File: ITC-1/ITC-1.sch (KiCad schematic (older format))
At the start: 84 parts, among them K1 кнопка, K2 кнопка, X1 крепеж, X2 крепеж

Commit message: упрощена схема подтяжек, раскинут разъем программирования
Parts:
- removed R19, R20, R24, R25: Резистор_0,065Вт, N_RLC:Резистор_SMD_0603_0,065_Вт_pnp, symbol elements:Резистор_0,065Вт
- added R41, R42: Резистор_0,065Вт, N_RLC:Резистор_SMD_0603_0,065_Вт_pnp, symbol elements:Резистор_0,065Вт
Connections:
- wire segments 303 -> 306
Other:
- moved on the sheet: C1, C2, G1, K1, K2, R21, R22, R32, R33, R34, R35, R36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

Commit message: раскинуты все разъемы, требуется подключить LED и поставить лого
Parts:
- removed R30, R31, R34, R35, R36: Резистор_0,065Вт, N_RLC:Резистор_SMD_0603_0,065_Вт_pnp, symbol elements:Резистор_0,065Вт
- removed VT12: Транзистор_полевой_N-IRLML6344TR, N_VD_HL:Транзистор_IRLML6344TR_SOT-23, symbol elements:Транзистор_полевой_N-IRLML6344TR
- G2: symbol MOTOR_2020_import:ИОП_LM4040BIM3-2.5_NOPB -> ITC-1-rescue:ИОП_LM4040BIM3-2.5_NOPB-MOTOR_2020_import
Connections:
- net labels removed: LED-DRIVE
- wire segments 306 -> 293
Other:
- moved on the sheet: R33, R37, R38, R39, R40

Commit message: готова трассировка, требуется контрольная проверка
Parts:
- added D1: LOGO, N_ICO:ni_10x10, symbol elements:LOGO
- added D2: LOGO, N_ICO:VLAD_10x10, symbol elements:LOGO
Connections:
- net BUTT_1: now also A1.30 (IO18); no longer A1.27 (IO16)
- net BUTT_2: now also A1.31 (IO19); no longer A1.28 (IO17)
- net LED_7: now also A1.27 (IO16); no longer A1.29 (IO5)
- net LED_8: now also A1.28 (IO17); no longer A1.30 (IO18)
- net LED_9: now also A1.29 (IO5); no longer A1.31 (IO19)
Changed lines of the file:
@@
 EESchema Schematic File Version 4
 LIBS:ITC-1-cache
-EELAYER 29 0
+EELAYER 30 0
 EELAYER END
 $Descr A2 23386 16535
@@
 Entry Wire Line
 	6500 2950 6400 3050
+Text Label 6250 3650 2    50   ~ 0
+LED_7
+Entry Wire Line
+	6500 3100 6400 3200
+Text Label 6250 3500 2    50   ~ 0
+LED_8
+Entry Wire Line
+	6500 3250 6400 3350
+Wire Wire Line
+	3100 4650 1350 4650
+Wire Wire Line
+	3100 4250 3100 4650
+Entry Wire Line
+	1250 4550 1350 4650
+Wire Wire Line
+	1500 4500 2950 4500
+Wire Wire Line
+	2950 4500 2950 4250
 Text Label 6250 3350 2    50   ~ 0
-LED_7
-Entry Wire Line
-	6500 3100 6400 3200
-Text Label 6250 3200 2    50   ~ 0
-LED_8
-Entry Wire Line
-	6500 3250 6400 3350
-Wire Wire Line
-	3100 4650 1350 4650
-Wire Wire Line
-	3100 4250 3100 4650
-Entry Wire Line
-	1250 4550 1350 4650
-Wire Wire Line
-	1500 4500 2950 4500
-Wire Wire Line
-	2950 4500 2950 4250
-Text Label 6250 3050 2    50   ~ 0
 LED_9
 Wire Wire Line
@@
 Entry Wire Line
 	6500 2900 6600 3000
-Text Label 6250 3650 2    50   ~ 0
+Text Label 6250 3200 2    50   ~ 0
 BUTT_1
-Text Label 6250 3500 2    50   ~ 0
+Text Label 6250 3050 2    50   ~ 0
 BUTT_2
 Wire Wire Line
@@
 Entry Wire Line
 	6400 3800 6500 3900
+Text Label 2875 13000 2    50   ~ 0
+3V3
+$Comp
+L elements:LOGO D1
+U 1 1 60B714C3
+P 4750 1000
+F 0 "D1" H 4675 1200 50  0001 C CNN
+F 1 "LOGO" H 4650 1000 50  0000 L CNN
+F 2 "N_ICO:ni_10x10" H 4750 1000 50  0001 C CNN
+F 3 "" H 4750 1000 50  0001 C CNN
+	1    4750 1000
+	1    0    0    -1
+$EndComp
+$Comp
+L elements:LOGO D2
+U 1 1 60BDB17A
+P 5250 1000
+F 0 "D2" H 5175 1200 50  0001 C CNN
+F 1 "LOGO" H 5150 1000 50  0000 L CNN
+F 2 "N_ICO:VLAD_10x10" H 5250 1000 50  0001 C CNN
+F 3 "" H 5250 1000 50  0001 C CNN
+	1    5250 1000
+	1    0    0    -1
+$EndComp
 Wire Bus Line
 	14500 1500 14500 4750
@@
 Wire Bus Line
 	1250 1500 1250 11750
-Text Label 2875 13000 2    50   ~ 0
-3V3
 $EndSCHEMATC

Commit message: добавлено отверстие для бондажа, требуется заменить светодиоды
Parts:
- added X3, X4, X5: крепеж, N_X:ОтверстиеD1.2, symbol elements:крепеж
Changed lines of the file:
@@
 L elements:LOGO D1
 U 1 1 60B714C3
-P 4750 1000
-F 0 "D1" H 4675 1200 50  0001 C CNN
-F 1 "LOGO" H 4650 1000 50  0000 L CNN
-F 2 "N_ICO:ni_10x10" H 4750 1000 50  0001 C CNN
-F 3 "" H 4750 1000 50  0001 C CNN
-	1    4750 1000
+P 5750 1000
+F 0 "D1" H 5675 1200 50  0001 C CNN
+F 1 "LOGO" H 5650 1000 50  0000 L CNN
+F 2 "N_ICO:ni_10x10" H 5750 1000 50  0001 C CNN
+F 3 "" H 5750 1000 50  0001 C CNN
+	1    5750 1000
 	1    0    0    -1
 $EndComp
@@
 L elements:LOGO D2
 U 1 1 60BDB17A
-P 5250 1000
-F 0 "D2" H 5175 1200 50  0001 C CNN
-F 1 "LOGO" H 5150 1000 50  0000 L CNN
-F 2 "N_ICO:VLAD_10x10" H 5250 1000 50  0001 C CNN
-F 3 "" H 5250 1000 50  0001 C CNN
-	1    5250 1000
+P 6250 1000
+F 0 "D2" H 6175 1200 50  0001 C CNN
+F 1 "LOGO" H 6150 1000 50  0000 L CNN
+F 2 "N_ICO:VLAD_10x10" H 6250 1000 50  0001 C CNN
+F 3 "" H 6250 1000 50  0001 C CNN
+	1    6250 1000
 	1    0    0    -1
 $EndComp
+$Comp
+L elements:крепеж X3
+U 1 1 60B5240E
+P 3750 1000
+F 0 "X3" H 3878 1046 50  0000 L CNN
+F 1 "крепеж" H 3878 955 50  0000 L CNN
+F 2 "N_X:ОтверстиеD1.2" H 3750 1000 50  0001 C CNN
+F 3 "" H 3750 1000 50  0001 C CNN
+	1    3750 1000
+	1    0    0    -1
+$EndComp
+$Comp
+L elements:крепеж X4
+U 1 1 60B8F90D
+P 4250 1000
+F 0 "X4" H 4378 1046 50  0000 L CNN
+F 1 "крепеж" H 4378 955 50  0000 L CNN
+F 2 "N_X:ОтверстиеD1.2" H 4250 1000 50  0001 C CNN
+F 3 "" H 4250 1000 50  0001 C CNN
+	1    4250 1000
+	1    0    0    -1
+$EndComp
+$Comp
+L elements:крепеж X5
+U 1 1 60BABF95
+P 4750 1000
+F 0 "X5" H 4878 1046 50  0000 L CNN
+F 1 "крепеж" H 4878 955 50  0000 L CNN
+F 2 "N_X:ОтверстиеD1.2" H 4750 1000 50  0001 C CNN
+F 3 "" H 4750 1000 50  0001 C CNN
+	1    4750 1000
+	1    0    0    -1
+$EndComp

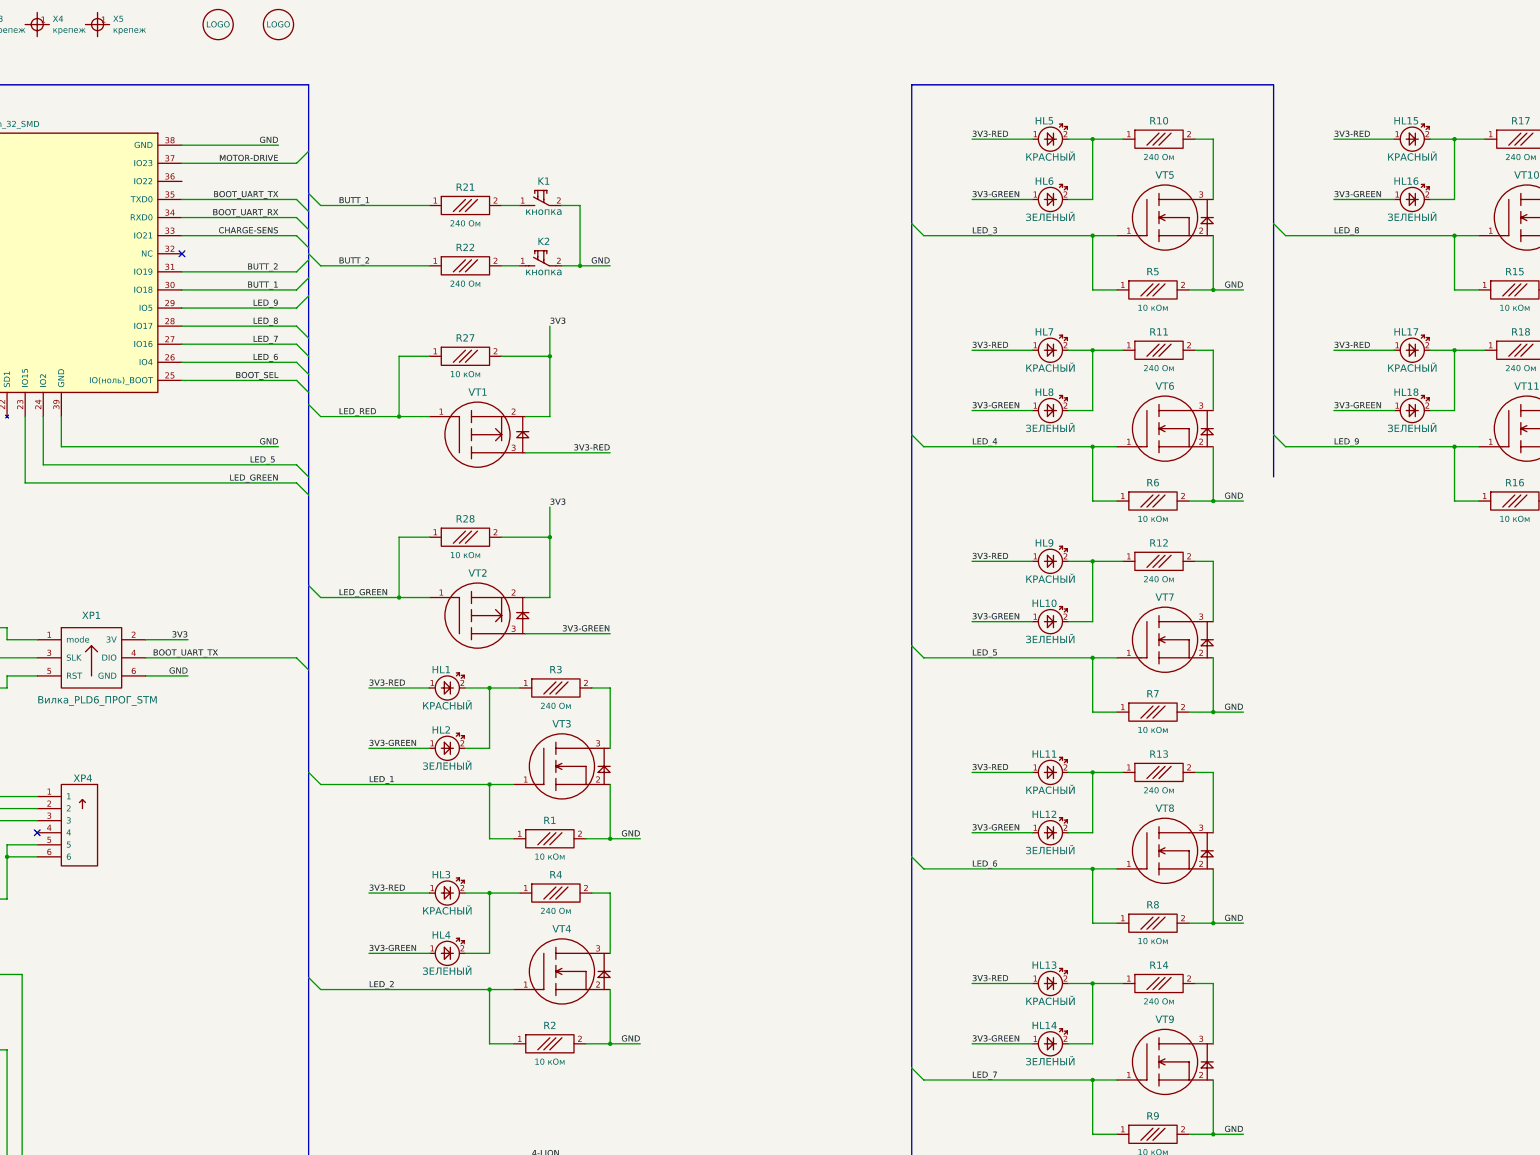
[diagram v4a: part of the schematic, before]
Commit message: заменены светодиоды на сдвоенные
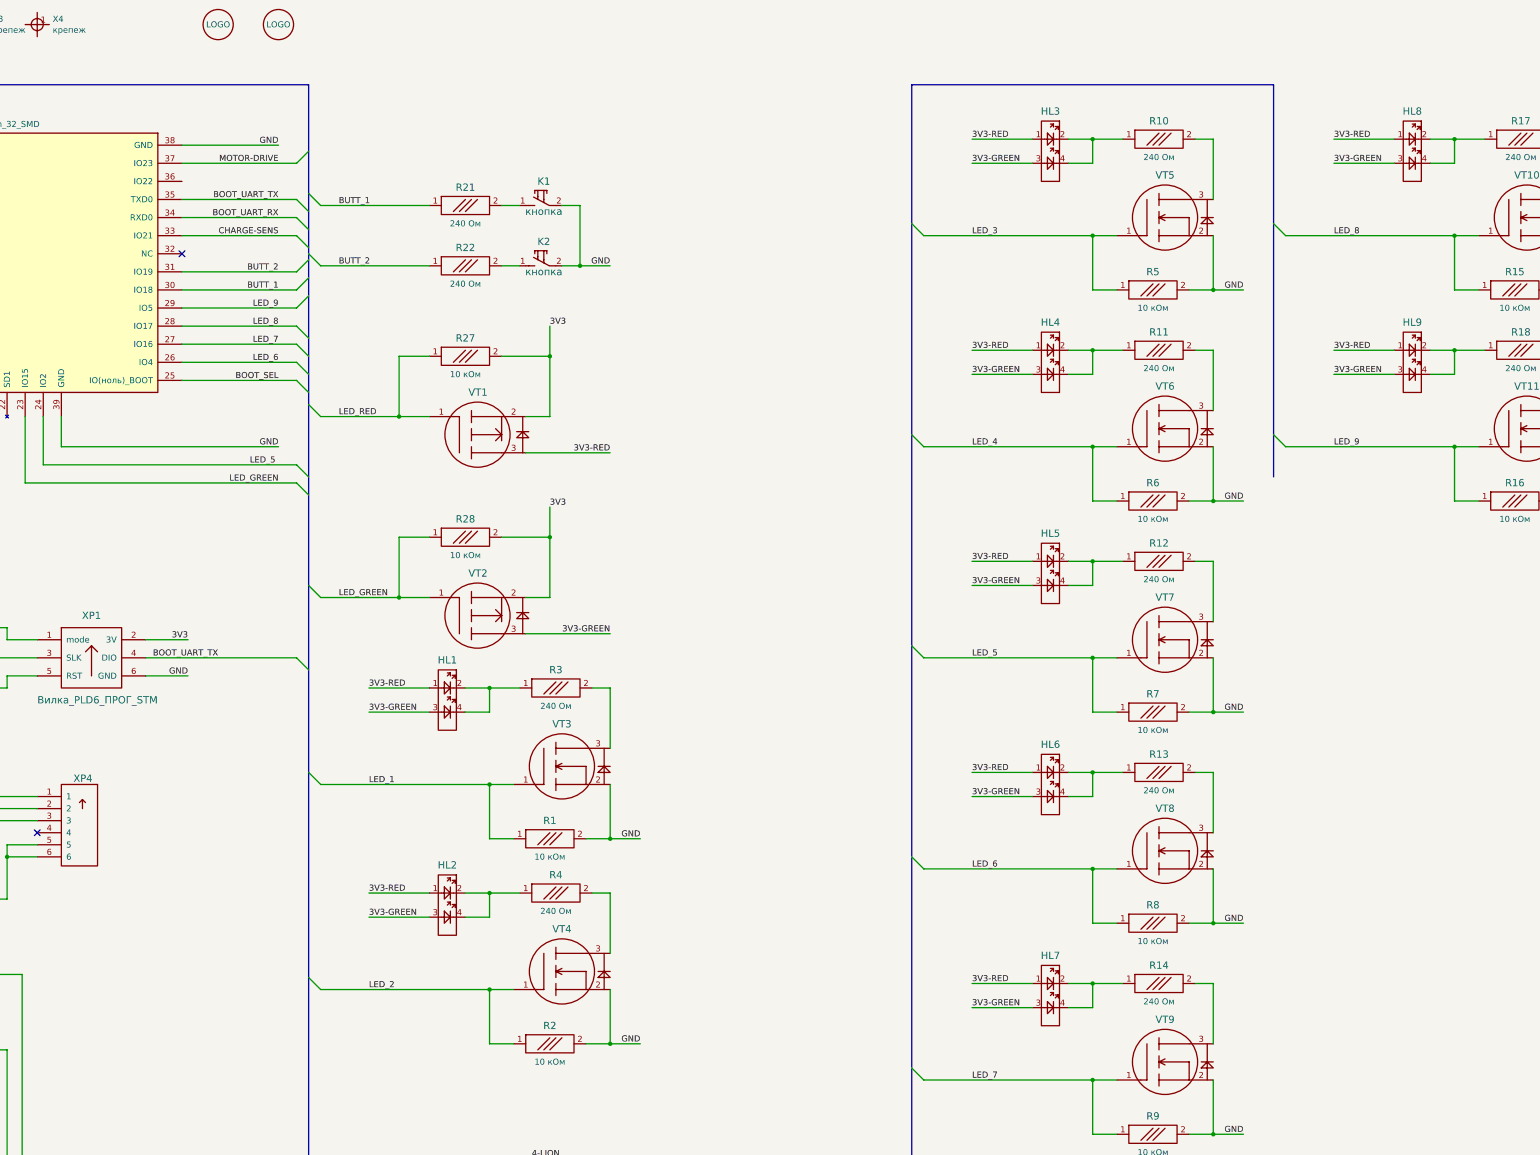
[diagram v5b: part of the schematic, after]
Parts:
- removed HL1, HL11, HL13, HL15, HL17, HL3, HL5, HL7, HL9: КРАСНЫЙ, N_VD_HL:Светодиод_SMD_0603, symbol elements:Светодиод
- removed HL10, HL12, HL14, HL16, HL18, HL2, HL4, HL6, HL8: ЗЕЛЕНЫЙ, N_VD_HL:Светодиод_SMD_0603, symbol elements:Светодиод
- removed X5: крепеж, N_X:ОтверстиеD1.2, symbol elements:крепеж
- added HL1, HL2, HL3, HL4, HL5, HL6, HL7, HL8, HL9: Светодиод_сдвоенный_KPB-3025SURKCGKC, N_VD_HL:Светодиод_SMD_m3025, symbol elements_2020:Светодиод_сдвоенный_KPB-3025SURKCGKC
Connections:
- net 3V3-GREEN: now also HL1.3, HL2.3, HL3.3, HL4.3, HL5.3, HL6.3, HL7.3, HL8.3, HL9.3
- net 3V3-RED: now also HL1.1, HL2.1, HL3.1, HL4.1, HL5.1, HL6.1, HL7.1, HL8.1, HL9.1
- net at R3.1: now also HL1.2, HL1.4
- net at R4.1: now also HL2.2, HL2.4
- net at R10.1: now also HL3.2, HL3.4
- net at R11.1: now also HL4.2, HL4.4
- net at R12.1: now also HL5.2, HL5.4
- net at R13.1: now also HL6.2, HL6.4
- net at R14.1: now also HL7.2, HL7.4
- net at R17.1: now also HL8.2, HL8.4
- net at R18.1: now also HL9.2, HL9.4

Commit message: закончена трассировка, сформированы герберы
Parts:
- added C3, C4, C5, C6: Конденсатор_керамический, N_RLC:Конденсатор_SMD_0603_pnp, symbol elements:Конденсатор_керамический
- added R19, R20, R24: Резистор_0,065Вт, N_RLC:Резистор_SMD_0603_0,065_Вт_pnp, symbol elements:Резистор_0,065Вт
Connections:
- net 1-LION: now also C6.1, R20.2; no longer A1.7 (IO35), R40.1
- net 2-LION: now also C5.1, R19.2; no longer A1.6 (IO34), R39.1
- net 3-LION: now also C4.1, R24.2; no longer A1.5 (SENSOR_VN), R38.1
- net 3V3: now also C3.1
- net GND: now also C3.2, C4.2, C5.2, C6.2
- new net ADC1-CH3: A1.5 (SENSOR_VN), R24.1, R38.1
- new net ADC1-CH6: A1.6 (IO34), R20.1, R39.1
- new net ADC1-CH7: A1.7 (IO35), R19.1, R40.1
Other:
- moved on the sheet: C2, R39, R40
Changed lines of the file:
@@
 L elements:Конденсатор_керамический C2
 U 1 1 60B8FB9B
-P 4500 12400
-F 0 "C2" V 4480 12488 60  0000 L CNN
-F 1 "Конденсатор_керамический" H 4600 12300 60  0001 C CNN
-F 2 "N_RLC:Конденсатор_SMD_0603_pnp" H 4500 12400 60  0001 C CNN
-F 3 "" H 4500 12400 60  0001 C CNN
-F 4 "10 мкФ/6,3 В" V 4578 12488 50  0000 L CNN "Номинал"
-F 5 "С111" H 4500 12400 50  0001 C CNN "УГО"
-	1    4500 12400
+P 4250 12400
+F 0 "C2" V 4230 12488 60  0000 L CNN
+F 1 "Конденсатор_керамический" H 4350 12300 60  0001 C CNN
+F 2 "N_RLC:Конденсатор_SMD_0603_pnp" H 4250 12400 60  0001 C CNN
+F 3 "" H 4250 12400 60  0001 C CNN
+F 4 "10 мкФ/6,3 В" V 4328 12488 50  0000 L CNN "Номинал"
+F 5 "С111" H 4250 12400 50  0001 C CNN "УГО"
+	1    4250 12400
 	0    1    1    0
 $EndComp
@@
 	2500 12750 3650 12750
 Wire Wire Line
-	4500 12750 4500 12500
+	4250 12750 4250 12500
 Wire Wire Line
 	3650 12550 3650 12750
-Connection ~ 3650 12750
-Wire Wire Line
-	3650 12750 4500 12750
 Wire Wire Line
 	3250 12250 2500 12250
@@
 	2500 12250 2500 12350
 Wire Wire Line
-	4050 12250 4500 12250
-Wire Wire Line
-	4500 12250 4500 12350
-Wire Wire Line
-	4500 12250 4750 12250
-Connection ~ 4500 12250
+	4250 12250 4250 12350
+Wire Wire Line
+	5000 12250 5250 12250
 Wire Wire Line
 	2500 12250 2000 12250
 Connection ~ 2500 12250
-Text Label 4750 12750 2    50   ~ 0
-GND
-Wire Wire Line
-	4750 12750 4500 12750
-Connection ~ 4500 12750
-Text Label 4750 12250 2    50   ~ 0
+Text Label 5250 12750 2    50   ~ 0
+GND
+Wire Wire Line
+	5250 12750 5000 12750
+Text Label 5250 12250 2    50   ~ 0
 3V3
 Text Label 2000 12250 0    50   ~ 0
@@
 Text Label 3500 10125 2    50   ~ 0
 3-LION
-Text Label 3500 9500 2    50   ~ 0
-2-LION
-Text Label 3500 8875 2    50   ~ 0
-1-LION
 $Comp
 L ITC-1-rescue:ИОП_LM4040BIM3-2.5_NOPB-MOTOR_2020_import G2
@@
 Text Label 1500 10125 0    50   ~ 0
 ADC1-CH3
+Text Label 1500 8875 0    50   ~ 0
+ADC1-CH6
 Text Label 1500 9500 0    50   ~ 0
-ADC1-CH6
-Text Label 1500 8875 0    50   ~ 0
 ADC1-CH7
 Text Label 1500 14000 0    50   ~ 0
@@
 	3325 10375 3500 10375
 Entry Wire Line
-	1250 9400 1350 9500
+	1250 8775 1350 8875
 $Comp
 L elements:Резистор_0,065Вт R39
 U 1 1 60E434FB
+P 3025 9125
+F 0 "R39" H 3025 9275 60  0000 C CNN
+F 1 "Резистор_0,065Вт" H 3025 8975 60  0001 C CNN
+F 2 "N_RLC:Резистор_SMD_0603_0,065_Вт_pnp" H 3025 9125 60  0001 C CNN
+F 3 "" H 3025 9125 60  0001 C CNN
+F 4 "R101" H 3025 9125 50  0001 C CNN "УГО"
+F 5 "10 кОм" H 3025 8975 50  0000 C CNN "Номинал"
+	1    3025 9125
+	1    0    0    -1
+$EndComp
+Wire Wire Line
+	1350 8875 2000 8875
+Wire Wire Line
+	2000 8875 2000 9125
+Wire Wire Line
+	2000 9125 2725 9125
+Connection ~ 2000 8875
+Text Label 3500 9125 2    50   ~ 0
+GND
+Wire Wire Line
+	3325 9125 3500 9125
+Entry Wire Line
+	1250 9400 1350 9500
+$Comp
+L elements:Резистор_0,065Вт R40
+U 1 1 60E5D454
 P 3025 9750
-F 0 "R39" H 3025 9900 60  0000 C CNN
+F 0 "R40" H 3025 9900 60  0000 C CNN
 F 1 "Резистор_0,065Вт" H 3025 9600 60  0001 C CNN
 F 2 "N_RLC:Резистор_SMD_0603_0,065_Вт_pnp" H 3025 9750 60  0001 C CNN
@@
 Wire Wire Line
 	3325 9750 3500 9750
-Entry Wire Line
-	1250 8775 1350 8875
-$Comp
-L elements:Резистор_0,065Вт R40
-U 1 1 60E5D454
-P 3025 9125
-F 0 "R40" H 3025 9275 60  0000 C CNN
-F 1 "Резистор_0,065Вт" H 3025 8975 60  0001 C CNN
-F 2 "N_RLC:Резистор_SMD_0603_0,065_Вт_pnp" H 3025 9125 60  0001 C CNN
-F 3 "" H 3025 9125 60  0001 C CNN
-F 4 "R101" H 3025 9125 50  0001 C CNN "УГО"
-F 5 "10 кОм" H 3025 8975 50  0000 C CNN "Номинал"
-	1    3025 9125
-	1    0    0    -1
-$EndComp
-Wire Wire Line
-	1350 8875 2000 8875
-Wire Wire Line
-	2000 8875 2000 9125
-Wire Wire Line
-	2000 9125 2725 9125
-Connection ~ 2000 8875
-Text Label 3500 9125 2    50   ~ 0
-GND
-Wire Wire Line
-	3325 9125 3500 9125
 Entry Wire Line
 	1250 11550 1350 11650
@@
 	3750 10750 3750 11000
 Wire Wire Line
-	2000 10125 3875 10125
+	2000 10125 2125 10125
 Wire Wire Line
 	3750 11000 3750 11550
@@
 	4000 11350 4250 11350
 Wire Wire Line
-	2000 9500 4000 9500
-Wire Wire Line
-	4125 8875 4125 11250
+	2000 8875 2125 8875
 Wire Wire Line
 	4125 11250 4250 11250
 Wire Wire Line
-	2000 8875 4125 8875
+	2000 9500 2125 9500
 Wire Wire Line
 	5450 3800 6400 3800
@@
 Wire Wire Line
 	16000 3900 16000 3700
+$Comp
+L elements:Резистор_0,065Вт R24
+U 1 1 60BB05C8
+P 2425 10125
+F 0 "R24" H 2425 10275 60  0000 C CNN
+F 1 "Резистор_0,065Вт" H 2425 9975 60  0001 C CNN
+F 2 "N_RLC:Резистор_SMD_0603_0,065_Вт_pnp" H 2425 10125 60  0001 C CNN
+F 3 "" H 2425 10125 60  0001 C CNN
+F 4 "R101" H 2425 10125 50  0001 C CNN "УГО"
+F 5 "10 кОм" H 2425 9975 50  0000 C CNN "Номинал"
+	1    2425 10125
+	1    0    0    -1
+$EndComp
+Wire Wire Line
+	2725 10125 3875 10125
+$Comp
+L elements:Резистор_0,065Вт R20
+U 1 1 60BB1788
+P 2425 8875
+F 0 "R20" H 2425 9025 60  0000 C CNN
+F 1 "Резистор_0,065Вт" H 2425 8725 60  0001 C CNN
+F 2 "N_RLC:Резистор_SMD_0603_0,065_Вт_pnp" H 2425 8875 60  0001 C CNN
+F 3 "" H 2425 8875 60  0001 C CNN
+F 4 "R101" H 2425 8875 50  0001 C CNN "УГО"
+F 5 "10 кОм" H 2425 8725 50  0000 C CNN "Номинал"
+	1    2425 8875
+	1    0    0    -1
+$EndComp
+$Comp
+L elements:Резистор_0,065Вт R19
+U 1 1 60BB21D7
+P 2425 9500
+F 0 "R19" H 2425 9650 60  0000 C CNN
+F 1 "Резистор_0,065Вт" H 2425 9350 60  0001 C CNN
+F 2 "N_RLC:Резистор_SMD_0603_0,065_Вт_pnp" H 2425 9500 60  0001 C CNN
+F 3 "" H 2425 9500 60  0001 C CNN
+F 4 "R101" H 2425 9500 50  0001 C CNN "УГО"
+F 5 "10 кОм" H 2425 9350 50  0000 C CNN "Номинал"
+	1    2425 9500
+	1    0    0    -1
+$EndComp
+Wire Wire Line
+	2725 9500 4000 9500
+Text Label 3500 8875 2    50   ~ 0
+1-LION
+Text Label 3500 9500 2    50   ~ 0
+2-LION
+Wire Wire Line
+	4125 8875 4125 11250
+Wire Wire Line
+	2725 8875 4125 8875
+$Comp
+L elements:Конденсатор_керамический C3
+U 1 1 60C6B107
+P 5000 12400
+F 0 "C3" V 4980 12488 60  0000 L CNN
+F 1 "Конденсатор_керамический" H 5100 12300 60  0001 C CNN
+F 2 "N_RLC:Конденсатор_SMD_0603_pnp" H 5000 12400 60  0001 C CNN
+F 3 "" H 5000 12400 60  0001 C CNN
+F 4 "10 мкФ/6,3 В" V 5078 12488 50  0000 L CNN "Номинал"
+F 5 "С111" H 5000 12400 50  0001 C CNN "УГО"
+	1    5000 12400
+	0    1    1    0
+$EndComp
+Wire Wire Line
+	5000 12500 5000 12750
+Wire Wire Line
+	5000 12750 4250 12750
+Connection ~ 5000 12750
+Wire Wire Line
+	5000 12350 5000 12250
+Wire Wire Line
+	5000 12250 4250 12250
+Connection ~ 5000 12250
+Wire Wire Line
+	4050 12250 4250 12250
+Connection ~ 4250 12250
+Wire Wire Line
+	4250 12750 3650 12750
+Connection ~ 4250 12750
+Connection ~ 3650 12750
+$Comp
+L elements:Конденсатор_керамический C4
+U 1 1 60D5EB05
+P 4500 10300
+F 0 "C4" V 4500 10200 60  0000 R CNN
+F 1 "Конденсатор_керамический" H 4600 10200 60  0001 C CNN
+F 2 "N_RLC:Конденсатор_SMD_0603_pnp" H 4500 10300 60  0001 C CNN
+F 3 "" H 4500 10300 60  0001 C CNN
+F 4 "1 мкФ/25 В" V 4600 10250 50  0000 R CNN "Номинал"
+F 5 "С111" H 4500 10300 50  0001 C CNN "УГО"
+	1    4500 10300
+	0    -1   1    0
+$EndComp
+Wire Wire Line
+	3875 10125 4500 10125
+Connection ~ 3875 10125
+Wire Wire Line
+	4500 10125 4500 10250
+Text Label 4750 10625 2    50   ~ 0
+GND
+Wire Wire Line
+	4500 10400 4500 10625
+$Comp
+L elements:Конденсатор_керамический C5
+U 1 1 60DD38A0
+P 5125 10300
+F 0 "C5" V 5125 10200 60  0000 R CNN
+F 1 "Конденсатор_керамический" H 5225 10200 60  0001 C CNN
+F 2 "N_RLC:Конденсатор_SMD_0603_pnp" H 5125 10300 60  0001 C CNN
+F 3 "" H 5125 10300 60  0001 C CNN
+F 4 "1 мкФ/25 В" V 5225 10250 50  0000 R CNN "Номинал"
+F 5 "С111" H 5125 10300 50  0001 C CNN "УГО"
+	1    5125 10300
+	0    -1   1    0
+$EndComp
+Wire Wire Line
+	5125 10400 5125 10625
+Wire Wire Line
+	4500 10625 5125 10625
+Wire Wire Line
+	4000 9500 5125 9500
+Wire Wire Line
+	5125 9500 5125 10250
+Connection ~ 4000 9500
+$Comp
+L elements:Конденсатор_керамический C6
+U 1 1 60E3D74E
+P 5750 10300
+F 0 "C6" V 5750 10200 60  0000 R CNN
+F 1 "Конденсатор_керамический" H 5850 10200 60  0001 C CNN
+F 2 "N_RLC:Конденсатор_SMD_0603_pnp" H 5750 10300 60  0001 C CNN
+F 3 "" H 5750 10300 60  0001 C CNN
+F 4 "1 мкФ/25 В" V 5850 10250 50  0000 R CNN "Номинал"
+F 5 "С111" H 5750 10300 50  0001 C CNN "УГО"
+	1    5750 10300
+	0    -1   1    0
+$EndComp
+Connection ~ 5125 10625
+Wire Wire Line
+	5750 10625 5750 10400
+Wire Wire Line
+	5125 10625 5750 10625
+Wire Wire Line
+	4125 8875 5750 8875
+Wire Wire Line
+	5750 8875 5750 10250
 Wire Bus Line
 	14500 1500 14500 4750
@@
 Wire Bus Line
 	1250 1500 1250 11750
+Connection ~ 4125 8875
 $EndSCHEMATC
